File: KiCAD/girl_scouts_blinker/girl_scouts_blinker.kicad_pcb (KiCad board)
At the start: 2 copper layers, 71.1 x 43.2 mm, 16 parts, among them SW1 SW_Push, SW2 SW_Push, SW3 SW_SPST, U1 ATtiny85-20P

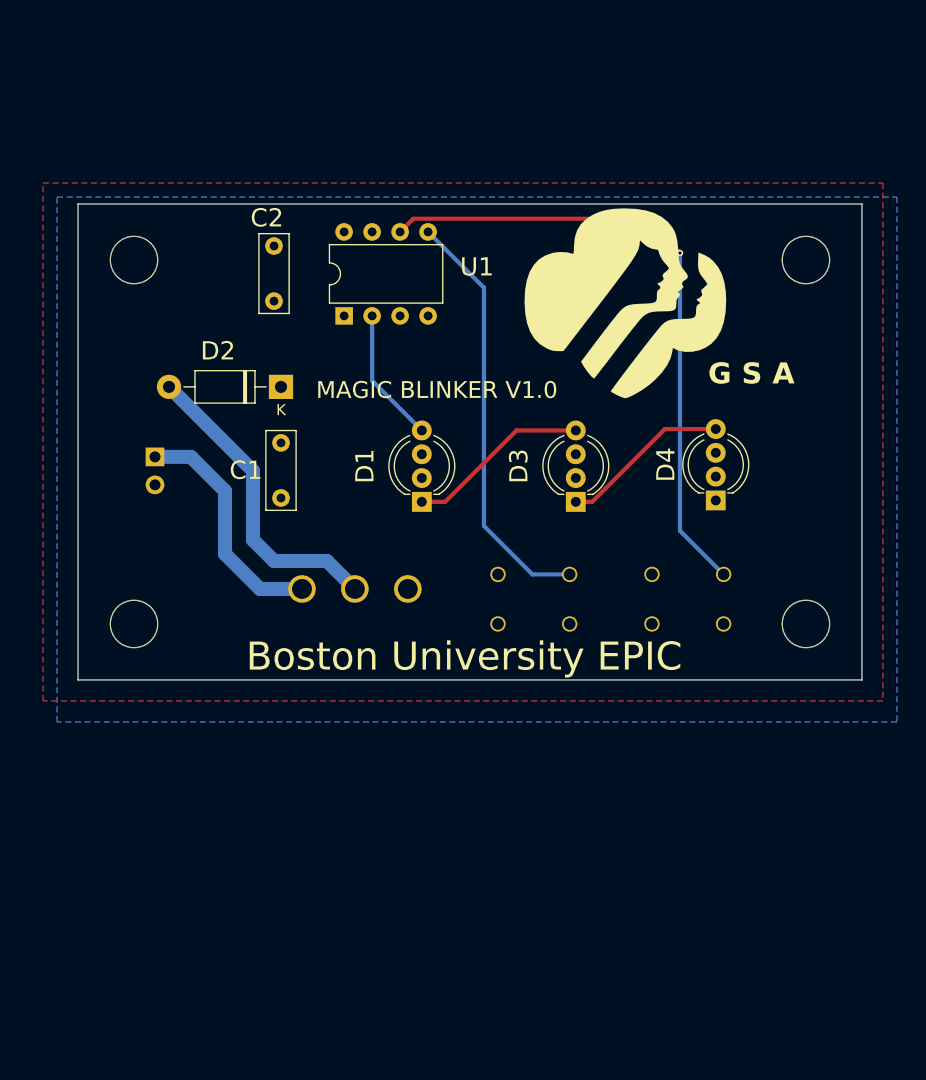
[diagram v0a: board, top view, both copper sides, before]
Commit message: add programming connector and RST R
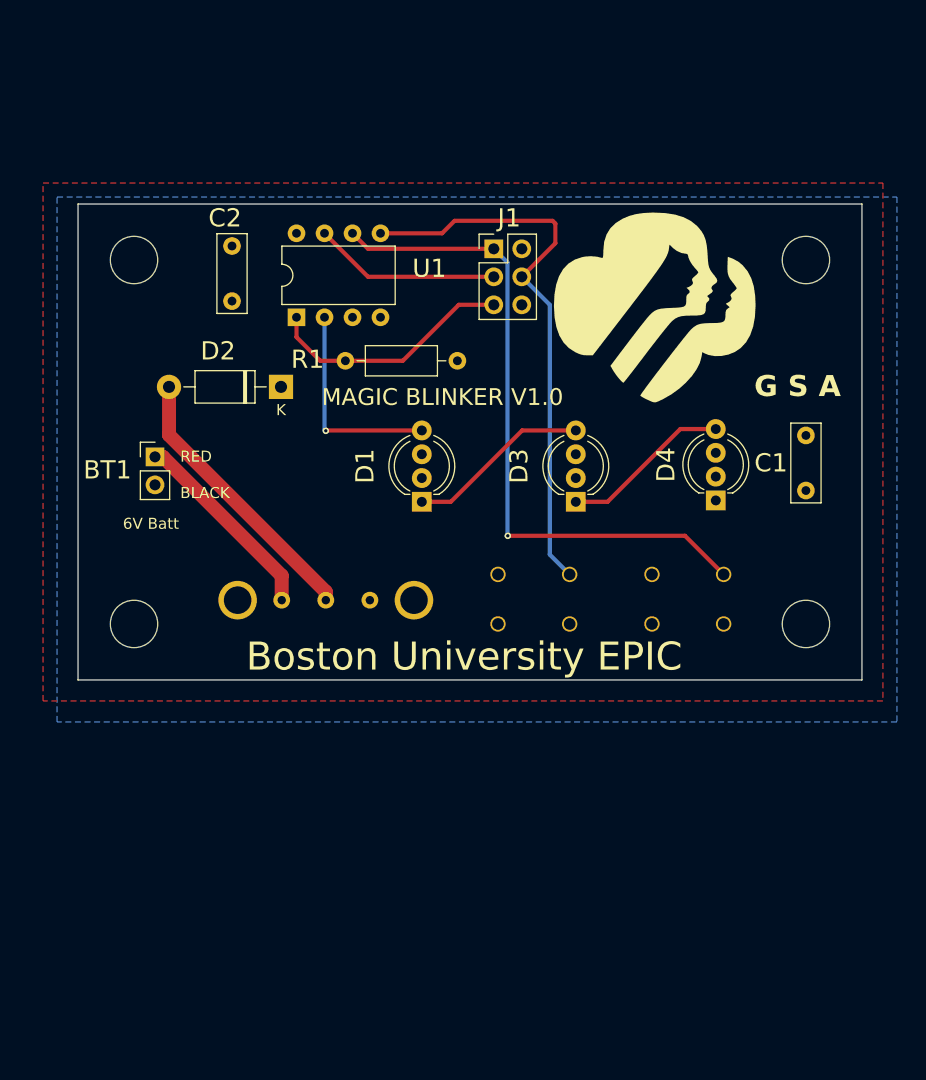
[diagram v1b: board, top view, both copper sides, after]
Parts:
- added J1: AVR-ISP-6, Connector_PinHeader_2.54mm:PinHeader_2x03_P2.54mm_Vertical, F.Cu at (80.9, 47.2)
- added R1: 10k, Resistor_THT:R_Axial_DIN0207_L6.3mm_D2.5mm_P10.16mm_Horizontal, F.Cu at (77.6, 57.4)
- BT1: moved to F.Cu
- D1, D3, D4: value NeoPixel_THT -> Adafruit NeoPixel_THT
- SW3: footprint my_slide_sw:sw_spdt_p4.8mm -> my_slide_sw:Slide_SLW-1711575-5A-N-D
- moved C1 47.6 mm to (109.2, 64.2)
- moved U1 4.32 mm to (63.0, 53.5)
- moved C2 3.81 mm to (57.1, 47.0)
- moved FID1 2.69 mm to (95.4, 52.5)
- moved SW3 2.39 mm to (65.7, 79.1)
- turned BT1 to 0 degrees
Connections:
- U1 pad 1: unconnected-(U1-~{RESET}/PB5-Pad1) -> /nRST
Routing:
- net /nRST: track 0.00 -> 22.7 mm
- net /SCK: track 0.00 -> 17.0 mm
- net /MOSI: track 38.4 -> 51.3 mm
- net Net-(D1-DIN): track 12.3 -> 19.1 mm, vias 0 -> 1
- net +6V: track 21.6 -> 18.2 mm
- net /MISO: track 58.0 -> 61.0 mm
- net Net-(D2-A): track 28.1 -> 25.2 mm
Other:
- board text added: "6V Batt"

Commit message: layout v1.1 done?
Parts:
- removed BT1: Battery, Connector_PinHeader_2.54mm:PinHeader_1x02_P2.54mm_Vertical
- removed D2: 1N4002, Diode_THT:D_DO-41_SOD81_P10.16mm_Horizontal
- added B1: BC9VPC, my_footprints:BC9VPC_MPD, F.Cu at (52.6, 53.7)
- added U2: LM7805_TO220, Package_TO_SOT_THT:TO-220-3_Horizontal_TabDown, F.Cu at (62.6, 74.9)
- D1, D3, D4: footprint LED_THT:LED_D5.0mm-4_RGB_Wide_Pins -> my_neopixel:LED_D5.0mm-4_RGB_Wide_Pins
- SW1, SW2: footprint push_sw:BTN-B3F-1000 -> my_cherry:SW_Cherry_MX_1.00u_PCB; moved to F.Cu
- SW3: moved to F.Cu
- moved H4 71.3 mm to (45.1, 112.4)
- moved H3 70.1 mm to (111.1, 112.4)
- moved R1 36.5 mm to (67.1, 92.3), turned to 90 degrees
- moved SW2 36.1 mm to (74.9, 101.0), turned to 0 degrees
- moved J1 35.3 mm to (108.6, 69.2)
- moved C2 32.4 mm to (80.6, 69.3)
- moved D1 28.6 mm to (53.3, 89.5)
- moved SW3 28.5 mm to (55.9, 105.9), turned to -90 degrees
- moved SW1 25.3 mm to (95.2, 101.0), turned to 0 degrees
- moved FID1 23.1 mm to (92.2, 75.3)
- moved U1 22.5 mm to (67.3, 75.6)
- moved D3 21.3 mm to (78.7, 89.2)
- moved D4 19.4 mm to (104.1, 89.2)
- moved C1 19.2 mm to (111.5, 83.2)
- moved H1 14.9 mm to (45.1, 33.7)
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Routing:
- net +6V: track 18.2 -> 56.8 mm
- net /SCK: track 17.0 -> 51.9 mm, vias 0 -> 2
- net /MOSI: track 51.3 -> 84.8 mm
- net /nRST: track 22.7 -> 49.5 mm
- net Net-(SW3-B): track 25.2 -> 49.0 mm
- net /MISO: track 61.0 -> 78.7 mm, vias 1 -> 2
- net Net-(D3-DOUT): track 15.4 -> 28.1 mm
- net Net-(D1-DOUT): track 16.7 -> 28.2 mm
- net Net-(D1-DIN): track 19.1 -> 19.6 mm, vias 1 -> 0
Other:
- board size 71.1 x 43.2 mm -> 76.2 x 88.9 mm
- board text removed: "6V Batt"
- board text removed: "BLACK"
- board text removed: "RED"

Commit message: ready to order?
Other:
- outline, holes or cut-outs redrawn
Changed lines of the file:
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@@
 		)
+	)
+	(gr_arc
+		(start 46.355 117.475)
+		(mid 41.864872 115.615128)
+		(end 40.005 111.125)
+		(stroke
+			(width 0)
+			(type default)
+		)
+		(layer "Edge.Cuts")
 	)
 	(gr_line
-		(start 116.205 28.575)
-		(end 116.205 117.475)
-		(stroke
-			(width 0.05)
+		(start 116.205 111.125)
+		(end 116.205 34.925)
+		(stroke
+			(width 0)
 			(type default)
 		)
@@
 	)
 	(gr_line
-		(start 40.005 117.475)
-		(end 40.005 28.575)
-		(stroke
-			(width 0.05)
+		(start 46.355 117.475)
+		(end 109.855 117.475)
+		(stroke
+			(width 0)
+			(type default)
+		)
+		(layer "Edge.Cuts")
+	)
+	(gr_arc
+		(start 109.855 28.575)
+		(mid 114.345128 30.434872)
+		(end 116.205 34.925)
+		(stroke
+			(width 0)
+			(type default)
+		)
+		(layer "Edge.Cuts")
+	)
+	(gr_arc
+		(start 40.005 34.925)
+		(mid 41.864872 30.434872)
+		(end 46.355 28.575)
+		(stroke
+			(width 0)
 			(type default)
 		)
@@
 	)
 	(gr_line
-		(start 116.205 117.475)
-		(end 40.005 117.475)
-		(stroke
-			(width 0.05)
+		(start 109.855 28.575)
+		(end 46.355 28.575)
+		(stroke
+			(width 0)
 			(type default)
 		)
@@
 	)
 	(gr_line
-		(start 40.005 28.575)
-		(end 116.205 28.575)
-		(stroke
-			(width 0.05)
+		(start 40.005 34.925)
+		(end 40.005 111.125)
+		(stroke
+			(width 0)
+			(type default)
+		)
+		(layer "Edge.Cuts")
+	)
+	(gr_arc
+		(start 116.205 111.125)
+		(mid 114.345128 115.615128)
+		(end 109.855 117.475)
+		(stroke
+			(width 0)
 			(type default)
 		)
@@
 		)
 	)
+	(dimension
+		(type orthogonal)
+		(layer "User.2")
+		(pts
+			(xy 40.005 28.575) (xy 116.205 28.575)
+		)
+		(height -4.699)
+		(orientation 0)
+		(gr_text "3.0000 in"
+			(at 78.105 22.726 0)
+			(layer "User.2")
+			(effects
+				(font
+					(size 1 1)
+					(thickness 0.15)
+				)
+			)
+		)
+		(format
+			(prefix "")
+			(suffix "")
+			(units 3)
+			(units_format 1)
+			(precision 4)
+		)
+		(style
+			(thickness 0.1)
+			(arrow_length 1.27)
+			(text_position_mode 0)
+			(extension_height 0.58642)
+			(extension_offset 0.5) keep_text_aligned)
+	)
+	(dimension
+		(type orthogonal)
+		(layer "User.2")
+		(pts
+			(xy 116.205 28.575) (xy 116.205 117.475)
+		)
+		(height 6.223)
+		(orientation 1)
+		(gr_text "3.5000 in"
+			(at 121.278 73.025 90)
+			(layer "User.2")
+			(effects
+				(font
+					(size 1 1)
+					(thickness 0.15)
+				)
+			)
+		)
+		(format
+			(prefix "")
+			(suffix "")
+			(units 3)
+			(units_format 1)
+			(precision 4)
+		)
+		(style
+			(thickness 0.1)
+			(arrow_length 1.27)
+			(text_position_mode 0)
+			(extension_height 0.58642)
+			(extension_offset 0.5) keep_text_aligned)
+	)
 	(segment
 		(start 46.355 95.885)
@@
 		)
 	)
+	(group ""
+		(members "1b4a5152-eb95-46c0-91e4-b52831a0b0ef" "685a2f30-5bfb-4a23-be71-7ee0164781c7"
+			"768e522c-9a87-40b1-949e-edccad7fcd53" "90a14ec8-76ef-43d8-84fd-2863adb905ee"
+			"9e610141-4882-4d76-a97c-c20f5a67cfc4" "c9e707d0-15e7-465c-bf4c-60968ceed895"
+			"da9ef64a-013c-4f5a-8d34-26cd5e955d21" "edfd8a89-caf5-4a08-9168-1fdaa2b38989"
+		)
+	)
